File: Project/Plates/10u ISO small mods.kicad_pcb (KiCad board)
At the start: 2 copper layers, 257.2 x 76.2 mm, 47 parts

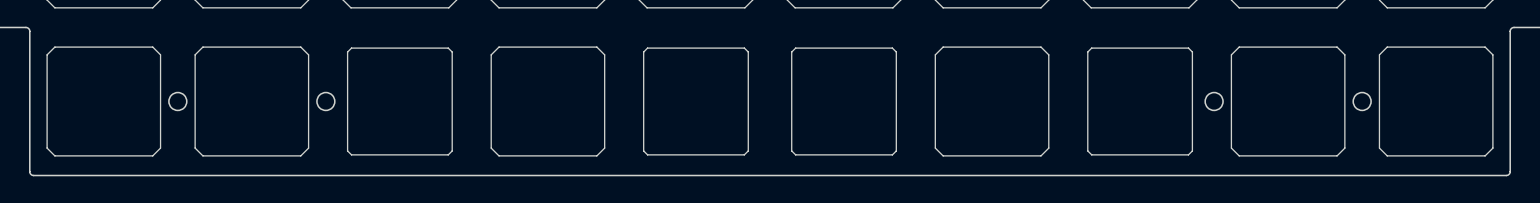
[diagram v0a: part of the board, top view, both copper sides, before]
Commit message: bottom row change, plate update, firmware update
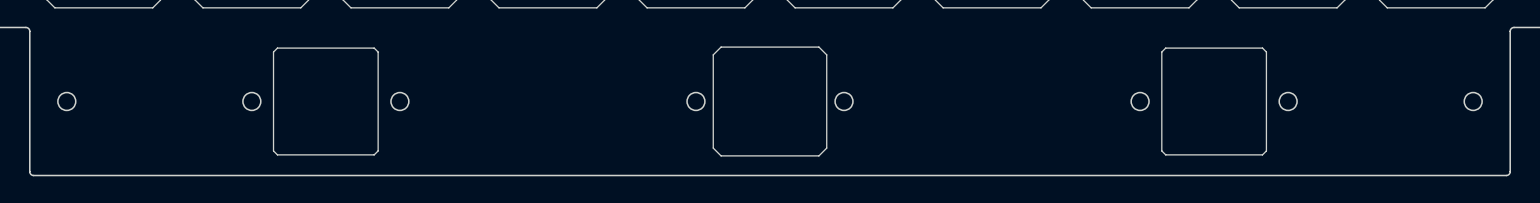
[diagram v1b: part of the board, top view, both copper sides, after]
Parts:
- removed the REF** at (79.4, 91.3)
- removed the REF** at (117.5, 91.3) (x2)
- removed the REF** at (174.6, 91.3) (x2)
- removed the REF** at (60.3, 91.3)
- removed the REF** at (231.8, 91.3)
- removed the REF** at (212.7, 91.3)
- added REF**: Value, cipulot_parts:ecs_plate_cut_1U, F.Cu at (146.1, 91.3)
- added REF**: Value, cipulot_parts:ecs_plate_cut_7U_space_stab, F.Cu at (146.1, 91.3)
- added REF**: Value, cipulot_parts:ecs_7U_space_stab, F.Cu at (146.1, 91.3)
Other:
- outline, holes or cut-outs redrawn
- board text added: "REF**"
- board text added: "SW_EC39"
